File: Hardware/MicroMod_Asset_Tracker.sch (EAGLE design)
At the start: 204 parts, among them IC1 SN74AVC4T774PW, IC2 SN74AVC4T774PW, IC3 SN74AVC4T774PW, J11 microSD, J13 TP, J17 NANO_SIM, J18 SARA_USB, J19 NI, J2 JTAG, J4 MICROMOD-2222-C, J5 SPI, J6 DIAG, J7 QWIIC_RIGHT_ANGLE, J9 !RST!, Q1 310mA/60V/1.6Ω, Q10 20V/0.2A/8MHz/1.2Ω/1Vth, Q2 310mA/60V/1.6Ω, Q3 310mA/60V/1.6Ω, Q4 310mA/60V/1.6Ω, Q5 20V/0.2A/8MHz/1.2Ω/1Vth, Q6 20V/4.2A/52mΩ/1.4W, Q7 310mA/60V/1.6Ω, U1 SARA-R5, U13 9DoF IMU, U14 1.8V/100mA, U2 MCP73831, U3 3.3V, U5 AP7361C-33FGE, U7 PCA9306, U8 74HC1G04

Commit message: Added the missing PROD_IDs
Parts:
- E3, E4: device New_Parts:ANTENNA-GROUNDEDEDGE_SMA_SMD -> SparkFun-RF:ANTENNA-GROUNDEDEDGE_SMA_SMD
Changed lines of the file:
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@@
 <part name="SUPPLY85" library="SparkFun-PowerSymbols" deviceset="3.3V" device=""/>
 <part name="SUPPLY87" library="SparkFun-PowerSymbols" deviceset="1.8V" device=""/>
-<part name="E3" library="New_Parts" deviceset="ANTENNA-GROUNDED" device="EDGE_SMA_SMD" value="LTE"/>
-<part name="E4" library="New_Parts" deviceset="ANTENNA-GROUNDED" device="EDGE_SMA_SMD" value="GNSS"/>
+<part name="E3" library="SparkFun-RF" deviceset="ANTENNA-GROUNDED" device="EDGE_SMA_SMD" value="LTE"/>
+<part name="E4" library="SparkFun-RF" deviceset="ANTENNA-GROUNDED" device="EDGE_SMA_SMD" value="GNSS"/>
 <part name="GND31" library="SparkFun-PowerSymbols" deviceset="GND" device=""/>
 <part name="GND32" library="SparkFun-PowerSymbols" deviceset="GND" device=""/>
@@
 <attribute name="VALUE" x="261.62" y="144.526" size="1.778" layer="96" align="top-center"/>
 </instance>
-<instance part="U$132" gate="G$1" x="40.64" y="101.6" smashed="yes">
+<instance part="U$132" gate="U1" x="40.64" y="101.6" smashed="yes">
 <attribute name="NAME" x="30.48" y="112.268" size="1.778" layer="95" font="vector"/>
 <attribute name="VALUE" x="30.48" y="88.9" size="1.778" layer="96" font="vector"/>
@@
 </segment>
 <segment>
-<pinref part="U$132" gate="G$1" pin="GND"/>
+<pinref part="U$132" gate="U1" pin="GND"/>
 <wire x1="27.94" y1="93.98" x2="25.4" y2="93.98" width="0.1524" layer="91"/>
 <pinref part="GND43" gate="1" pin="GND"/>
 <wire x1="25.4" y1="93.98" x2="25.4" y2="91.44" width="0.1524" layer="91"/>
-<pinref part="U$132" gate="G$1" pin="CTG"/>
+<pinref part="U$132" gate="U1" pin="CTG"/>
 <wire x1="27.94" y1="99.06" x2="25.4" y2="99.06" width="0.1524" layer="91"/>
 <wire x1="25.4" y1="99.06" x2="25.4" y2="93.98" width="0.1524" layer="91"/>
@@
 </segment>
 <segment>
-<pinref part="U$132" gate="G$1" pin="QSTRT"/>
+<pinref part="U$132" gate="U1" pin="QSTRT"/>
 <wire x1="50.8" y1="93.98" x2="53.34" y2="93.98" width="0.1524" layer="91"/>
 <pinref part="GND76" gate="1" pin="GND"/>
@@
 <net name="V_BATT" class="0">
 <segment>
-<pinref part="U$132" gate="G$1" pin="CELL"/>
+<pinref part="U$132" gate="U1" pin="CELL"/>
 <wire x1="27.94" y1="104.14" x2="25.4" y2="104.14" width="0.1524" layer="91"/>
 <pinref part="SUPPLY25" gate="G$1" pin="V_BATT"/>
 <wire x1="25.4" y1="104.14" x2="25.4" y2="109.22" width="0.1524" layer="91"/>
-<pinref part="U$132" gate="G$1" pin="VDD"/>
+<pinref part="U$132" gate="U1" pin="VDD"/>
 <wire x1="25.4" y1="109.22" x2="25.4" y2="111.76" width="0.1524" layer="91"/>
 <wire x1="27.94" y1="109.22" x2="25.4" y2="109.22" width="0.1524" layer="91"/>
@@
 <net name="I2C_SCL" class="0">
 <segment>
-<pinref part="U$132" gate="G$1" pin="SCL"/>
+<pinref part="U$132" gate="U1" pin="SCL"/>
 <wire x1="50.8" y1="99.06" x2="53.34" y2="99.06" width="0.1524" layer="91"/>
 <label x="53.34" y="99.06" size="1.27" layer="95" xref="yes"/>
@@
 <net name="I2C_SDA" class="0">
 <segment>
-<pinref part="U$132" gate="G$1" pin="SDA"/>
+<pinref part="U$132" gate="U1" pin="SDA"/>
 <wire x1="50.8" y1="104.14" x2="53.34" y2="104.14" width="0.1524" layer="91"/>
 <label x="53.34" y="104.14" size="1.27" layer="95" xref="yes"/>

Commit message: Updates for V11 of the PCB
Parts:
- removed R13: 100k, SparkFun-Resistors:100KOHM-0603-1/10W-1%
- added VIN/3: JUMPER-SMT_2_NC_TRACE_SILK, SparkFun-Jumpers:JUMPER-SMT_2_NC_TRACE_SILK
- R33: value 470 -> 100; device SparkFun-Resistors:470OHM-0603-1/10W-1% -> SparkFun-Resistors:100OHM-0603-1/10W-1%
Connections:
- new net N$18: R10.2, VIN/3.1
- net !BOOT!: no longer R13.1
- net 3.3V: no longer R13.2
- net VIN: now also VIN/3.2; no longer R10.2
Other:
- note added: "v11"
- note removed: "v10"
- moved on the sheet: H5, R10, R9, S2, S3

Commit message: v11
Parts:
- removed D9: 3.3V, SparkFun-DiscreteSemi:DIODE-ZENER-MM3Z3V3T1G
- removed JP19: JUMPER-SMT_2_NC_TRACE_SILK, SparkFun-Jumpers:JUMPER-SMT_2_NC_TRACE_SILK
- removed JP21: JUMPER-SMT_2_NO_SILK, SparkFun-Jumpers:JUMPER-SMT_2_NO_SILK
- added JP9: JUMPER-SMT_2_NC_TRACE_SILK, SparkFun-Jumpers:JUMPER-SMT_2_NC_TRACE_SILK
- added Q8, Q9: 310mA/60V/1.6Ω, SparkFun-DiscreteSemi:MOSFET-NCH-2N7002PW
- added R13: 1k, SparkFun-Resistors:1KOHM-0603-1/10W-1%
- added R45: 100k, SparkFun-Resistors:100KOHM-0603-1/10W-1%
- JP13, JP14, JP15, JP16, JP17: value JUMPER-SMT_2_NC_TRACE_SILK -> JUMPER-SMT_2_NO_SILK; device SparkFun-Jumpers:JUMPER-SMT_2_NC_TRACE_SILK -> SparkFun-Jumpers:JUMPER-SMT_2_NO_SILK
- R35: value 1k -> 470; device SparkFun-Resistors:1KOHM-0603-1/10W-1% -> SparkFun-Resistors:470OHM-0603-1/10W-1%
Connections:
- removed net G10: J4.G10/ADC_D+/CAM_VSYNC, JP19.1
- removed net G9: J4.G9/ADC_D-/CAM_HSYNC, JP21.1
- new net ANT_REG_EN: Q9.D, R45.2, U3.EN
- new net N$19: J4.I2C_!INT!, JP9.2
- new net N$40: Q8.G, R13.2
- new net N$42: Q8.D, Q9.G, R25.2
- net 3.3V: now also R25.1, R45.1
- net ANT_GNSS_PWR_EN: now also R13.1, U1.GPIO2; no longer D9.C, JP16.2, R25.2, U3.EN
- net GND: now also Q8.S, Q9.S; no longer D9.A
- net ICM_INT: now also JP9.1; no longer J4.I2C_!INT!
- net SARA_!ON!: now also JP16.2; no longer JP19.2, JP21.2
- net VIN: no longer R25.1
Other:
- note added: "ANT_GNSS_PWR_EN is 1.8V (from SARA GPIO2). To minimise power draw when the SARA is OFF, ANT_REG_EN needs to be low when ANT_GNSS_PWR_EN is low."
- note added: "GNSS Active Antenna Power Enable"
- moved on the sheet: R25

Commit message: Updated files for v11 after production review
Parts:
- removed TP11: TEST-POINT3, SparkFun-Connectors:TEST-POINT3
- added JP19: JUMPER-SMT_3_1-NC_TRACE_SILK, SparkFun-Jumpers:JUMPER-SMT_3_1-NC_TRACE_SILK
- renumbered U$132 to U4
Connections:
- removed net SARA_INT_1.8V: Q5.S, R29.1, TP11.1, U1.EXT_INT
- new net N$43: JP19.2, Q5.S, R29.1
- new net SARA_EXT_INT: JP19.3, U1.EXT_INT
- new net SARA_GPIO3: JP19.1, U1.GPIO3
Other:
- note added: "Conductor Spacing: 16mil / 0.63mm"
- note added: "Conductor Width: 12mil / 0.47mm"
- note added: "Copper Thickness: 1oz"
- note added: "Differential Pair Calculation:"
- note added: "Material: FR-4 STD Er: 4.6"
- note added: "Plating Thickness: 1oz"
- note added: "Prepreg dielectric thickness: 0.2mm (8mil)"
- note added: "SARA VCCIO is 1.8V"
- note added: "Zdifferential: 89 Ohms"
- note added: "https://saturnpcb.com/pcb_toolkit/"
- moved on the sheet: C6, D5, D7, H5, J1, J15, J16, J2, R14, R2, R21, R3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

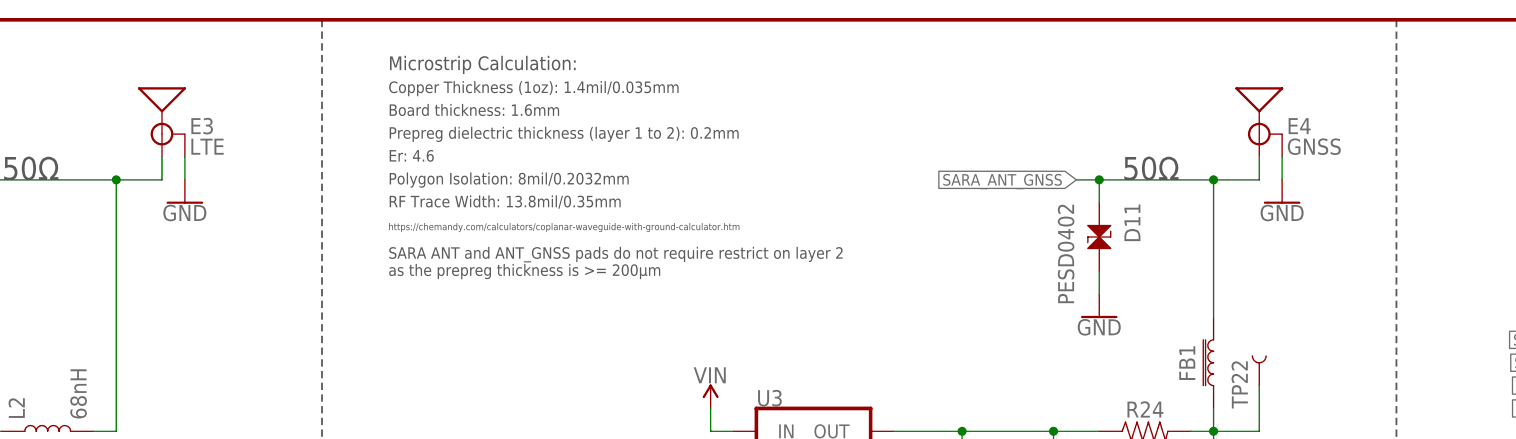
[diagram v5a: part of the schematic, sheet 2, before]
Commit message: Adding the PROD_ID for the SARA-R510M8S
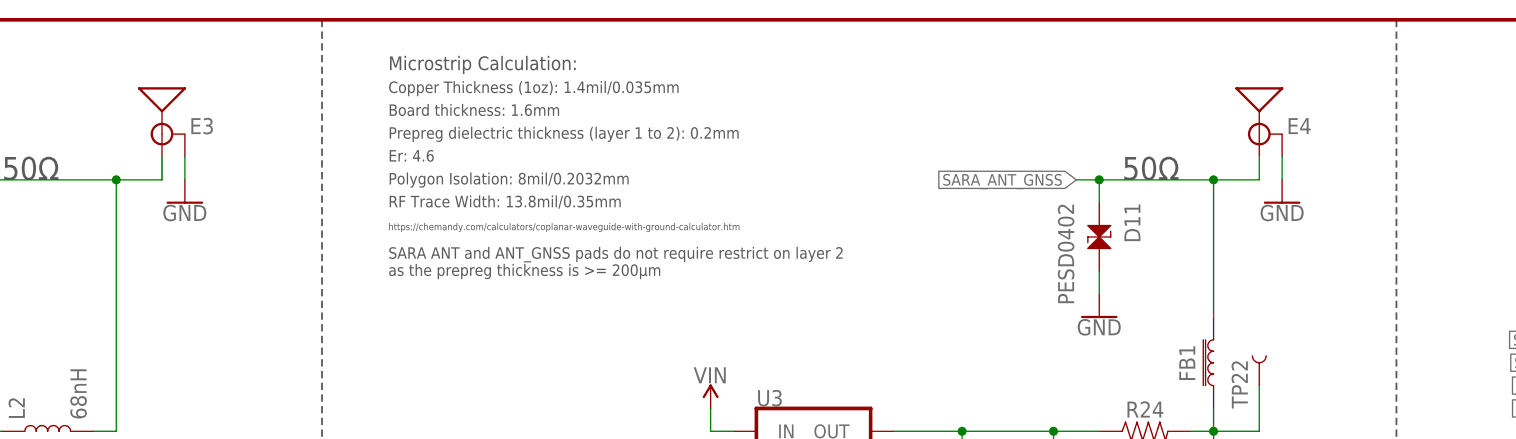
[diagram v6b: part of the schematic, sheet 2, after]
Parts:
- E3: value LTE -> ANTENNA-SMA-GROUNDEDEDGE_SMA_SMD; device SparkFun-RF:ANTENNA-GROUNDEDEDGE_SMA_SMD -> SparkFun-RF:ANTENNA-SMA-GROUNDEDEDGE_SMA_SMD
- E4: value GNSS -> ANTENNA-SMA-GROUNDEDEDGE_SMA_SMD; device SparkFun-RF:ANTENNA-GROUNDEDEDGE_SMA_SMD -> SparkFun-RF:ANTENNA-SMA-GROUNDEDEDGE_SMA_SMD
- U1: value SARA-R5 -> SARA-R510M8S; device SARA_R5:SARA-R5 -> SARA_R5:SARA-R510M8S
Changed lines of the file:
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@@
 <part name="SUPPLY29" library="SparkFun-PowerSymbols" deviceset="3.3V" device=""/>
 <part name="GND41" library="SparkFun-PowerSymbols" deviceset="GND" device=""/>
-<part name="U1" library="SARA_R5" deviceset="SARA-R5" device=""/>
+<part name="U1" library="SARA_R5" deviceset="SARA-R510M8S" device="" value="SARA-R510M8S"/>
 <part name="U13" library="SparkFun-Sensors" deviceset="ICM-20948" device="" value="9DoF IMU"/>
 <part name="C51" library="SparkFun-Capacitors" deviceset="0.1UF" device="-0603-25V-5%" value="0.1uF"/>
@@
 <part name="SUPPLY85" library="SparkFun-PowerSymbols" deviceset="3.3V" device=""/>
 <part name="SUPPLY87" library="SparkFun-PowerSymbols" deviceset="1.8V" device=""/>
-<part name="E3" library="SparkFun-RF" deviceset="ANTENNA-GROUNDED" device="EDGE_SMA_SMD" value="LTE"/>
-<part name="E4" library="SparkFun-RF" deviceset="ANTENNA-GROUNDED" device="EDGE_SMA_SMD" value="GNSS"/>
 <part name="GND31" library="SparkFun-PowerSymbols" deviceset="GND" device=""/>
 <part name="GND32" library="SparkFun-PowerSymbols" deviceset="GND" device=""/>
@@
 <part name="GND77" library="SparkFun-PowerSymbols" deviceset="GND" device=""/>
 <part name="JP19" library="SparkFun-Jumpers" deviceset="JUMPER-SMT_3_1-NC_TRACE" device="_SILK" package3d_urn="urn:adsk.eagle:package:39288/1"/>
+<part name="E3" library="SparkFun-RF" deviceset="ANTENNA-SMA-GROUNDED" device="EDGE_SMA_SMD"/>
+<part name="E4" library="SparkFun-RF" deviceset="ANTENNA-SMA-GROUNDED" device="EDGE_SMA_SMD"/>
 </parts>
 <sheets>
@@
 <instances>
 <instance part="FRAME2" gate="G$1" x="0" y="0" smashed="yes"/>
-<instance part="E4" gate="G$1" x="195.58" y="266.7" smashed="yes">
-<attribute name="NAME" x="198.628" y="266.7" size="1.778" layer="95" font="vector"/>
-<attribute name="VALUE" x="198.628" y="264.414" size="1.778" layer="96" font="vector"/>
-</instance>
 <instance part="GND31" gate="1" x="198.12" y="259.08" smashed="yes">
 <attribute name="VALUE" x="198.12" y="258.826" size="1.778" layer="96" align="top-center"/>
 </instance>
-<instance part="E3" gate="G$1" x="73.66" y="266.7" smashed="yes">
-<attribute name="NAME" x="76.708" y="266.7" size="1.778" layer="95" font="vector"/>
-<attribute name="VALUE" x="76.708" y="264.414" size="1.778" layer="96" font="vector"/>
-</instance>
 <instance part="GND32" gate="1" x="76.2" y="259.08" smashed="yes">
 <attribute name="VALUE" x="76.2" y="258.826" size="1.778" layer="96" align="top-center"/>
@@
 <attribute name="NAME" x="358.14" y="154.559" size="1.778" layer="95" font="vector" rot="R180"/>
 </instance>
+<instance part="E3" gate="G$1" x="73.66" y="266.7" smashed="yes">
+<attribute name="NAME" x="76.708" y="266.7" size="1.778" layer="95" font="vector"/>
+</instance>
+<instance part="E4" gate="G$1" x="195.58" y="266.7" smashed="yes">
+<attribute name="NAME" x="198.628" y="266.7" size="1.778" layer="95" font="vector"/>
+</instance>
 </instances>
 <busses>
@@
 <net name="GND" class="0">
 <segment>
-<pinref part="GND31" gate="1" pin="GND"/>
-<pinref part="E4" gate="G$1" pin="GND"/>
-<wire x1="198.12" y1="261.62" x2="198.12" y2="264.16" width="0.1524" layer="91"/>
-</segment>
-<segment>
-<pinref part="GND32" gate="1" pin="GND"/>
-<pinref part="E3" gate="G$1" pin="GND"/>
-<wire x1="76.2" y1="261.62" x2="76.2" y2="264.16" width="0.1524" layer="91"/>
-</segment>
-<segment>
 <pinref part="L1" gate="G$1" pin="2"/>
 <pinref part="GND45" gate="1" pin="GND"/>
@@
 <wire x1="154.94" y1="86.36" x2="154.94" y2="83.82" width="0.1524" layer="91"/>
 </segment>
+<segment>
+<pinref part="E3" gate="G$1" pin="GND"/>
+<pinref part="GND32" gate="1" pin="GND"/>
+<wire x1="76.2" y1="264.16" x2="76.2" y2="261.62" width="0.1524" layer="91"/>
+</segment>
+<segment>
+<pinref part="E4" gate="G$1" pin="GND"/>
+<pinref part="GND31" gate="1" pin="GND"/>
+<wire x1="198.12" y1="264.16" x2="198.12" y2="261.62" width="0.1524" layer="91"/>
+</segment>
 </net>
 <net name="SARA_ANT" class="0">
@@
 <pinref part="C18" gate="G$1" pin="2"/>
 <wire x1="50.8" y1="261.62" x2="68.58" y2="261.62" width="0.1524" layer="91"/>
-<pinref part="E3" gate="G$1" pin="SIGNAL"/>
 <wire x1="68.58" y1="261.62" x2="73.66" y2="261.62" width="0.1524" layer="91"/>
-<wire x1="73.66" y1="261.62" x2="73.66" y2="264.16" width="0.1524" layer="91"/>
 <pinref part="L2" gate="G$1" pin="2"/>
 <wire x1="66.04" y1="233.68" x2="68.58" y2="233.68" width="0.1524" layer="91"/>
 <wire x1="68.58" y1="233.68" x2="68.58" y2="261.62" width="0.1524" layer="91"/>
 <junction x="68.58" y="261.62"/>
+<pinref part="E3" gate="G$1" pin="SIGNAL"/>
+<wire x1="73.66" y1="264.16" x2="73.66" y2="261.62" width="0.1524" layer="91"/>
 </segment>
 </net>
@@
 <net name="SARA_ANT_GNSS" class="0">
 <segment>
-<pinref part="E4" gate="G$1" pin="SIGNAL"/>
-<wire x1="195.58" y1="264.16" x2="195.58" y2="261.62" width="0.1524" layer="91"/>
 <wire x1="195.58" y1="261.62" x2="190.5" y2="261.62" width="0.1524" layer="91"/>
 <label x="175.26" y="261.62" size="1.27" layer="95" rot="R180" xref="yes"/>
@@
 <wire x1="177.8" y1="259.08" x2="177.8" y2="261.62" width="0.1524" layer="91"/>
 <junction x="177.8" y="261.62"/>
+<pinref part="E4" gate="G$1" pin="SIGNAL"/>
+<wire x1="195.58" y1="264.16" x2="195.58" y2="261.62" width="0.1524" layer="91"/>
 </segment>
 </net>
